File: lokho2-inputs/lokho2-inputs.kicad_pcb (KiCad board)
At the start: 2 copper layers, 100 x 100 mm, 60 parts, among them J1 SWITCHES, Q1 BC846, SW1 SW_DIP_x04, U1 74HC85, U2 MCP23S17_SP, U3 74AHC04, U4 74AHC04, U5 74AHC04

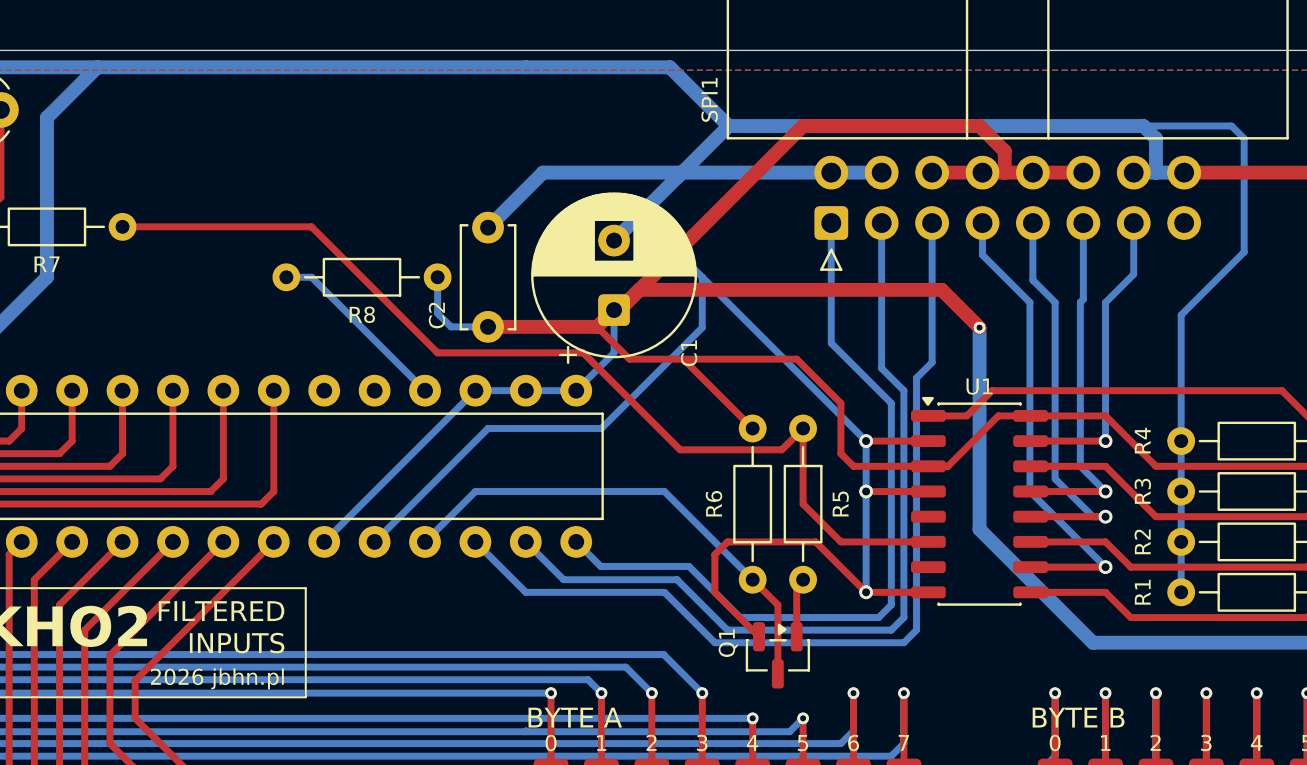
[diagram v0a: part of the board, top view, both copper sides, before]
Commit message: added INT-GP connection option
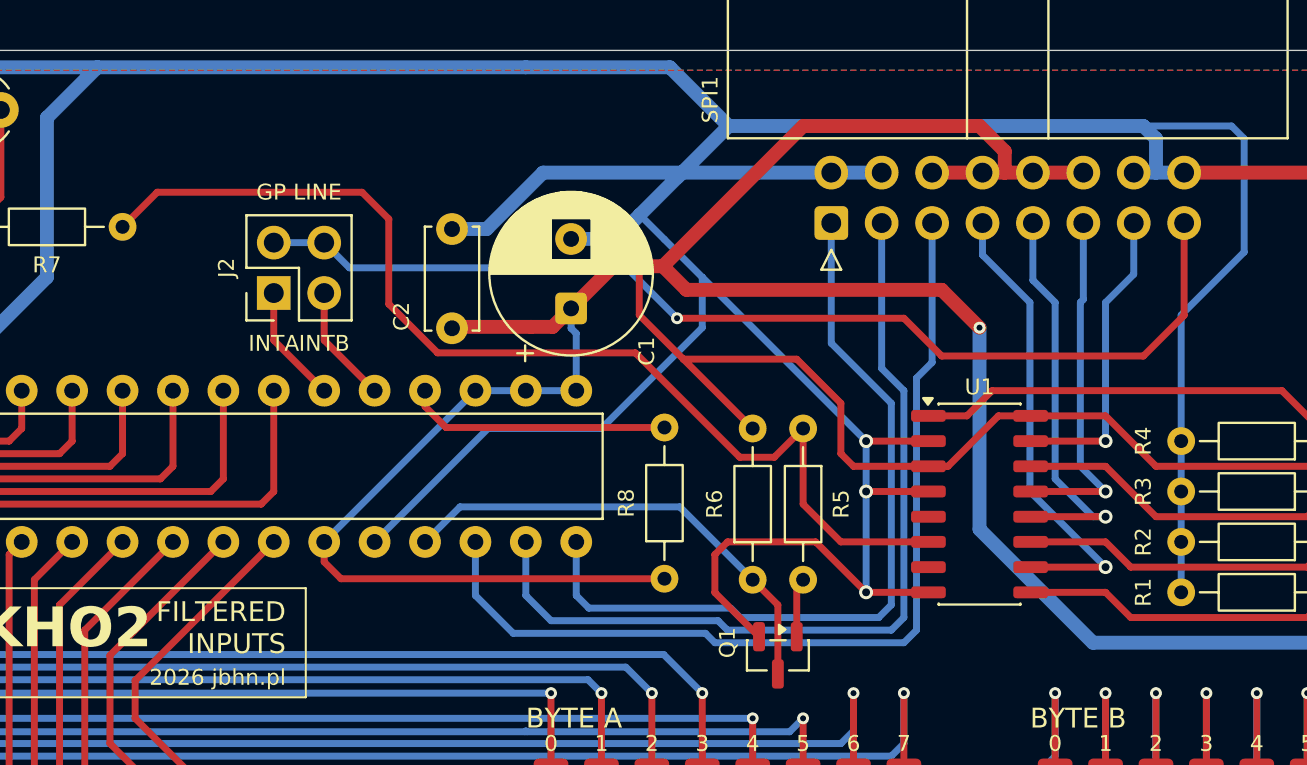
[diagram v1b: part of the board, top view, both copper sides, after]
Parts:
- added J2: INT, Connector_PinHeader_2.54mm:PinHeader_2x02_P2.54mm_Vertical, F.Cu at (133.0, 72.2)
- moved R8 19.0 mm to (152.7, 86.6), turned to 90 degrees
- moved C1 2.17 mm to (148.0, 73.0)
- moved C2 1.82 mm to (142.0, 69.0)
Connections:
- U2 pad 19: unconnected-(U2-INTB-Pad19) -> INTB
- U2 pad 20: unconnected-(U2-INTA-Pad20) -> INTA
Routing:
- net GP: track 0.00 -> 53.7 mm, vias 0 -> 1
- net +3V3: track 386.9 -> 401.1 mm
- net INTB: track 0.00 -> 5.97 mm
- net INTA: track 0.00 -> 5.97 mm
- net Net-(U1-Oa=b): track 50.3 -> 54.6 mm
- net GND: track 638.8 -> 642.7 mm
- net Net-(U2-~{RESET}): track 9.35 -> 13.3 mm
- net SPI_MISO: track 38.2 -> 39.8 mm
- net SPI_MOSI: track 41.5 -> 43.1 mm
- net SPI_SCK: track 45.4 -> 47.0 mm
- net ADDR_SEL: track 24.7 -> 24.0 mm
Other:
- board text added: "GP LINE"
- board text added: "INTA"
- board text added: "INTB"
